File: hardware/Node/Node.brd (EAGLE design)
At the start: 49.5 x 49.5 mm, 71 parts, among them J1 AVR_SPI_PRG_6NS, J2 M04X2, Q1 PMR280UN, Q2 PMR280UN, Q3 PMR280UN, SW1 KSS, SW2 KSS, U1 ATMEGA32U4QFN, U2 BLUETOOTH-RN41", U3 LSM303DLM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

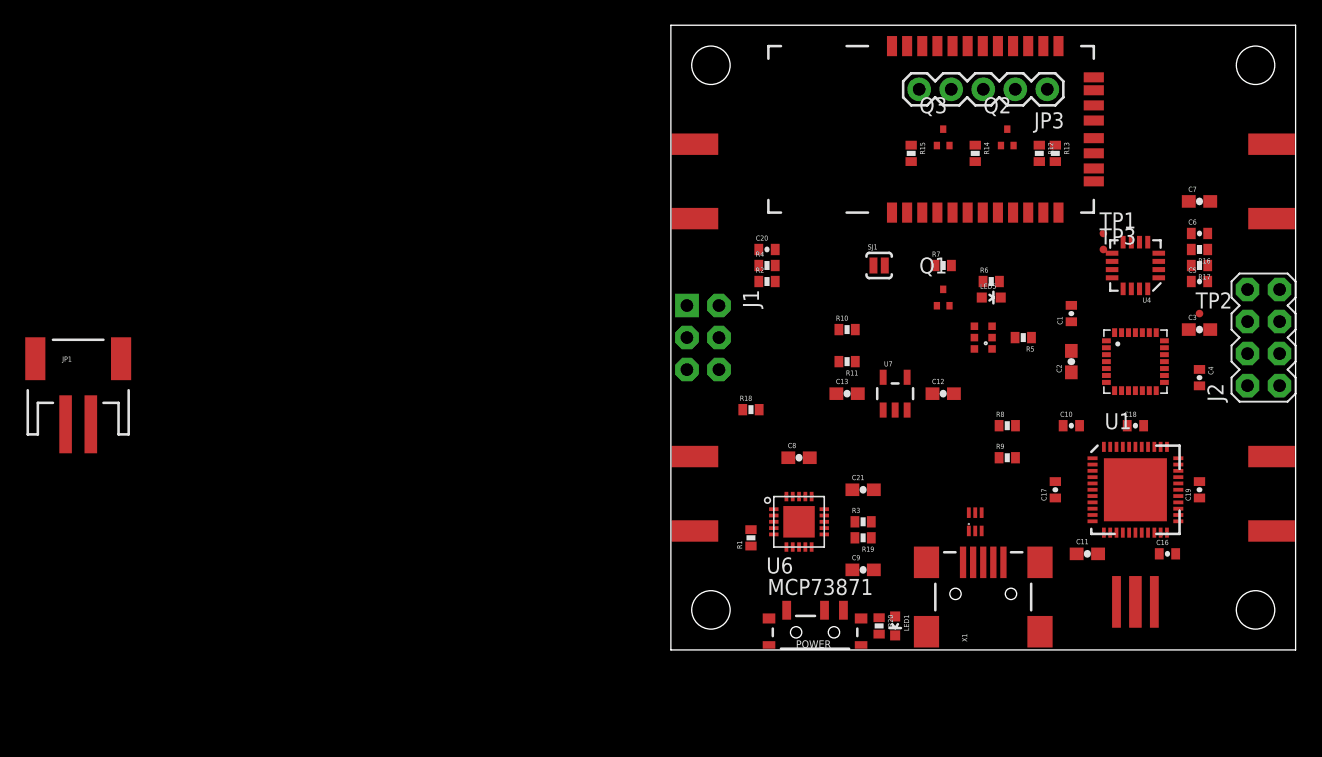
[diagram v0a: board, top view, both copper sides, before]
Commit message: put vbus on the header
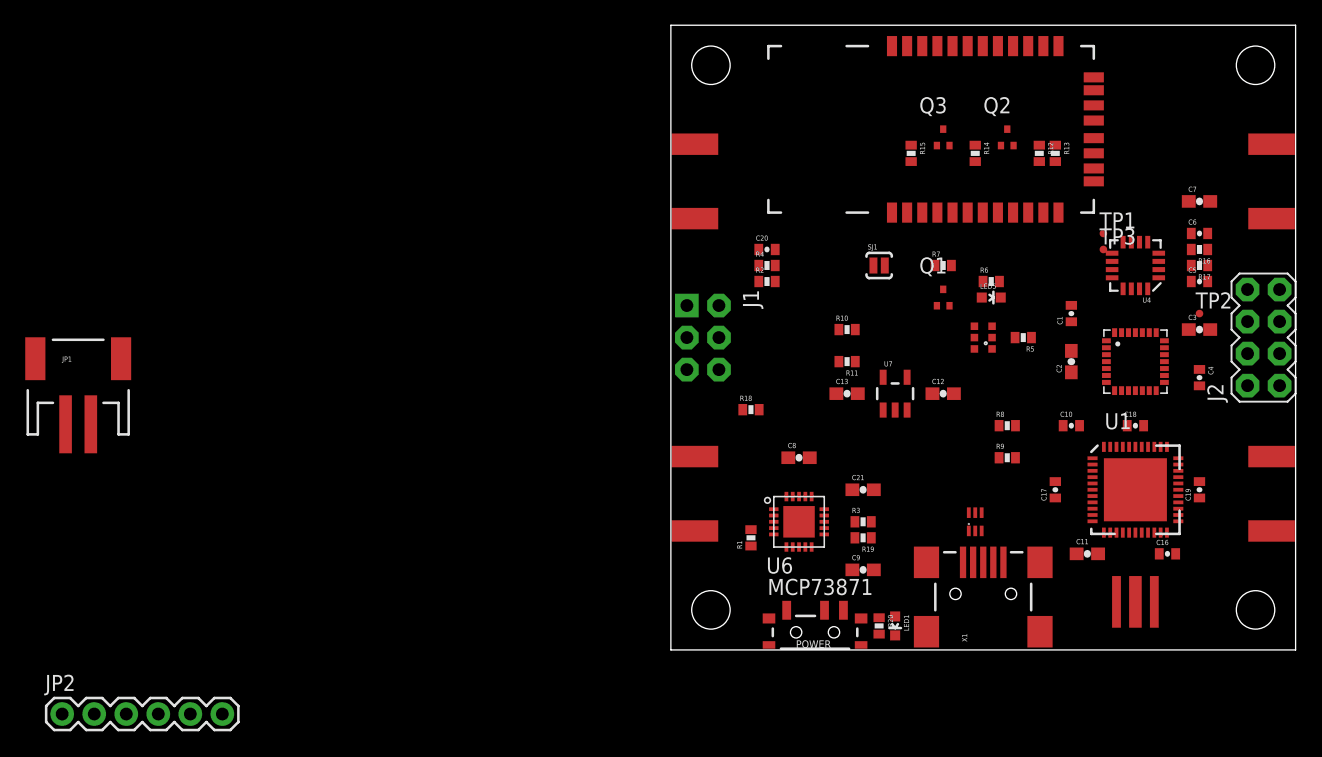
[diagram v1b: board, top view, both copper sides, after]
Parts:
- removed JP3: (no value), SparkFun:1X05
- added JP2: (no value), SparkFun:1X06
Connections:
- net +3V3: now also JP2.2; no longer JP3.1
- net GND: now also JP2.6; no longer JP3.5
- net RX_I: now also JP2.4; no longer JP3.3
- net TX_O: now also JP2.5; no longer JP3.4
- net VBUS: now also JP2.1
- net VIN: now also JP2.3; no longer JP3.2

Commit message: Start of laying out traces
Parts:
- moved JP2 81.1 mm to (17.8, 41.9)
- moved JP1 56.6 mm to (9.53, 24.8), turned to 90 degrees
- moved LED1 16.7 mm to (1.91, 6.99), turned to 270 degrees
- moved C5 15.2 mm to (41.9, 44.5), turned to 90 degrees
- moved R20 14.5 mm to (5.08, 10.8)
- moved R10 12.5 mm to (20.3, 14.6)
- moved R11 12.0 mm to (20.3, 12.7)
- moved C6 11.5 mm to (40.6, 44.5), turned to 90 degrees
- moved U4 10.8 mm to (41.9, 40.0), turned to 0 degrees
- moved R15 9.52 mm to (28.6, 39.4), turned to 180 degrees
- moved C7 9.44 mm to (38.7, 44.5), turned to 90 degrees
- moved TP1 9.25 mm to (43.2, 35.6)
- moved Q3 9.09 mm to (29.8, 44.5), turned to 90 degrees
- moved C13 8.98 mm to (20.3, 26.7)
- moved C8 7.75 mm to (14.6, 8.89)
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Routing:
- net VBUS: track 0.00 -> 13.0 mm
- net N$4: track 0.00 -> 7.32 mm
- net N$2: track 0.00 -> 6.11 mm
- net N$1: track 0.00 -> 5.90 mm
- net N$13: track 0.00 -> 4.47 mm
- net N$16: track 0.00 -> 2.69 mm
- net D-: track 0.00 -> 2.50 mm
- net D+: track 0.00 -> 2.49 mm
- net N$36: track 0.00 -> 2.49 mm
- net N$19: track 0.00 -> 2.45 mm
- added copper zone on layer 1, net N$11
- added copper zone on layer 1, net N$4
- added copper zone on layer 1, net VBUS

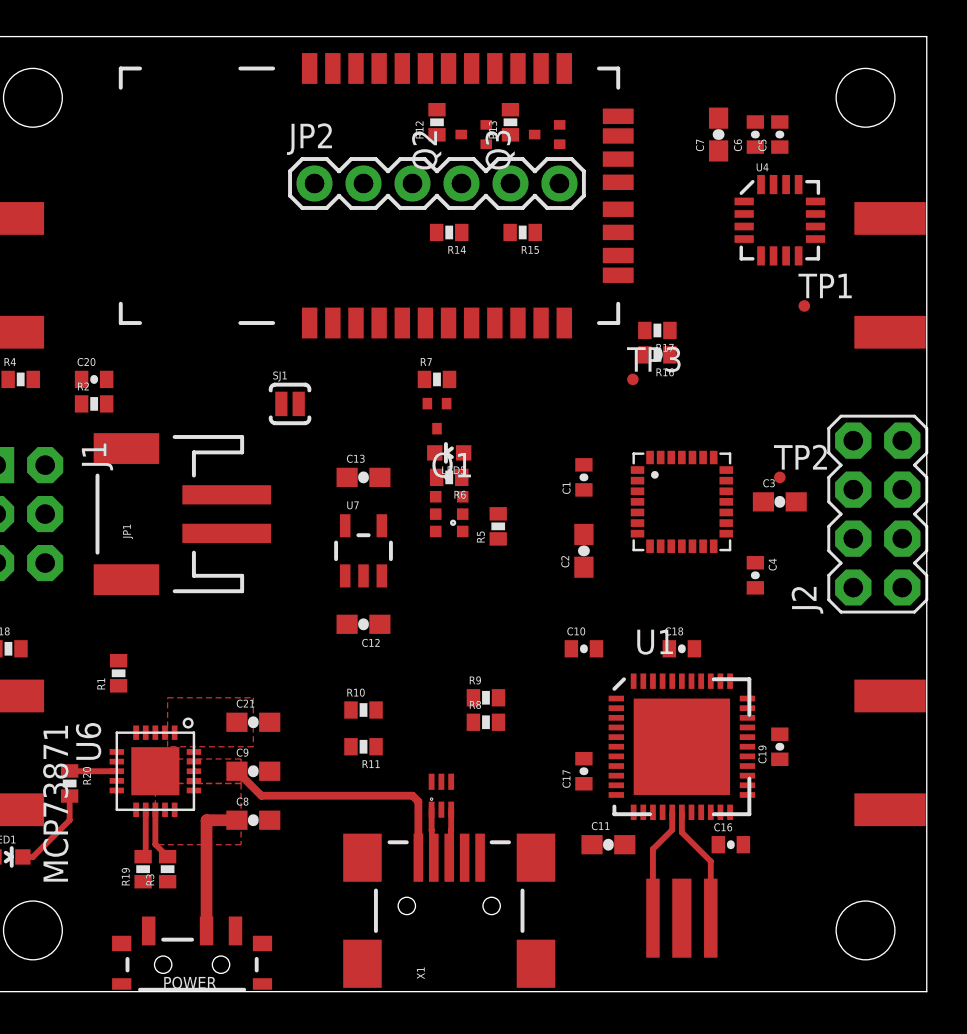
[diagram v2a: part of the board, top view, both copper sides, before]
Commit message: Routing more of the easy traces
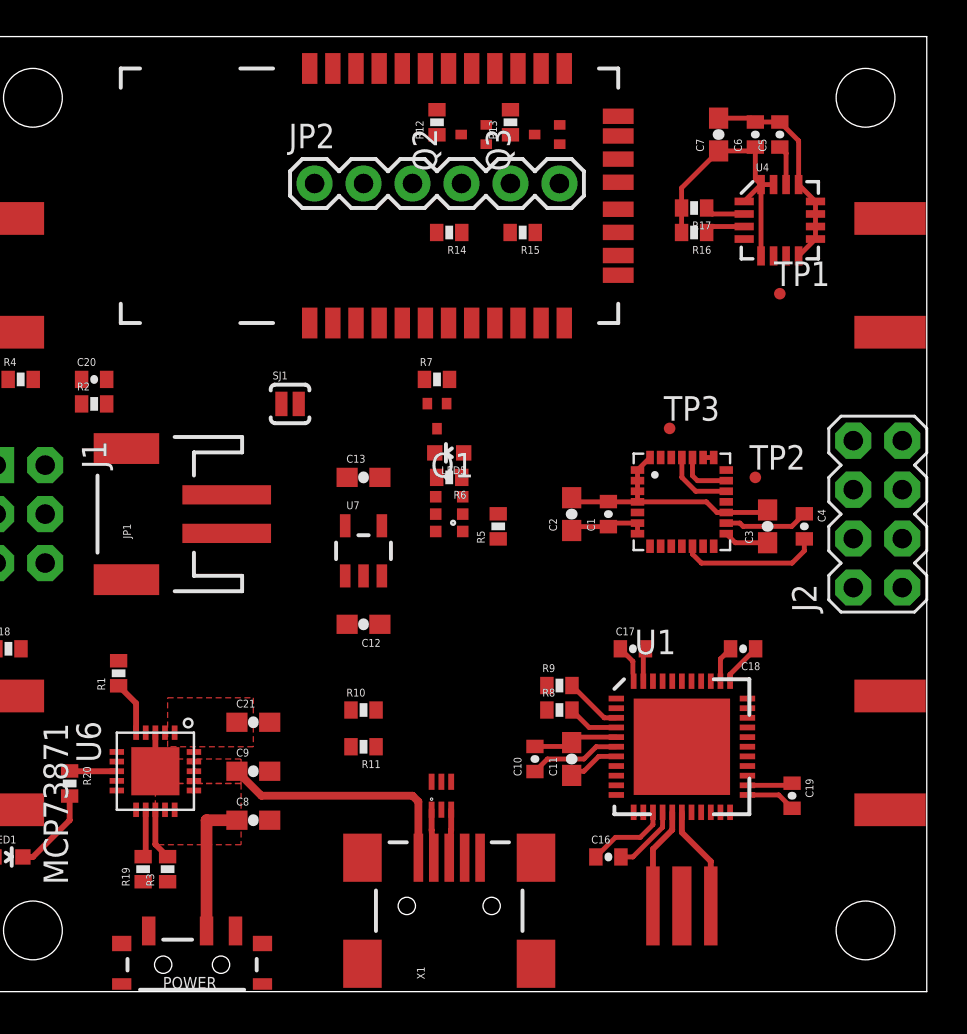
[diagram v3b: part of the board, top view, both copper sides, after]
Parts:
- moved C17 6.84 mm to (34.3, 17.8), turned to 0 degrees
- moved R17 6.63 mm to (37.5, 40.6)
- moved R16 6.63 mm to (37.5, 39.4)
- moved C16 6.38 mm to (33.0, 6.99)
- moved C10 6.25 mm to (29.2, 12.1), turned to 90 degrees
- moved C11 4.84 mm to (31.1, 12.1), turned to 90 degrees
- moved R8 3.86 mm to (30.5, 14.6)
- moved R9 3.86 mm to (30.5, 15.9)
- moved C4 3.59 mm to (43.2, 24.1)
- moved C18 3.18 mm to (40.0, 17.8), turned to 180 degrees
- moved TP3 3.18 mm to (36.2, 29.2)
- moved C19 2.62 mm to (42.5, 10.2), turned to 270 degrees
- moved C1 2.29 mm to (33.0, 24.8)
- moved C2 2.01 mm to (31.1, 24.8)
- moved TP1 1.42 mm to (41.9, 36.2)
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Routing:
- net GND: track 0.00 -> 40.6 mm
- net +3V3: track 0.00 -> 34.5 mm
- net N$6: track 0.00 -> 7.29 mm
- net SDA: track 0.00 -> 5.70 mm
- net SCL: track 0.00 -> 4.89 mm
- net N$5: track 0.00 -> 4.39 mm
- net N$24: track 0.00 -> 2.99 mm
- net N$8: track 0.00 -> 2.80 mm
- net VBUS: track 13.0 -> 15.7 mm
- net N$23: track 0.00 -> 2.69 mm
- net N$3: track 0.00 -> 2.34 mm
- net N$7: track 0.00 -> 2.08 mm
- net N$2: track 6.11 -> 5.48 mm
- net N$1: track 5.90 -> 5.27 mm

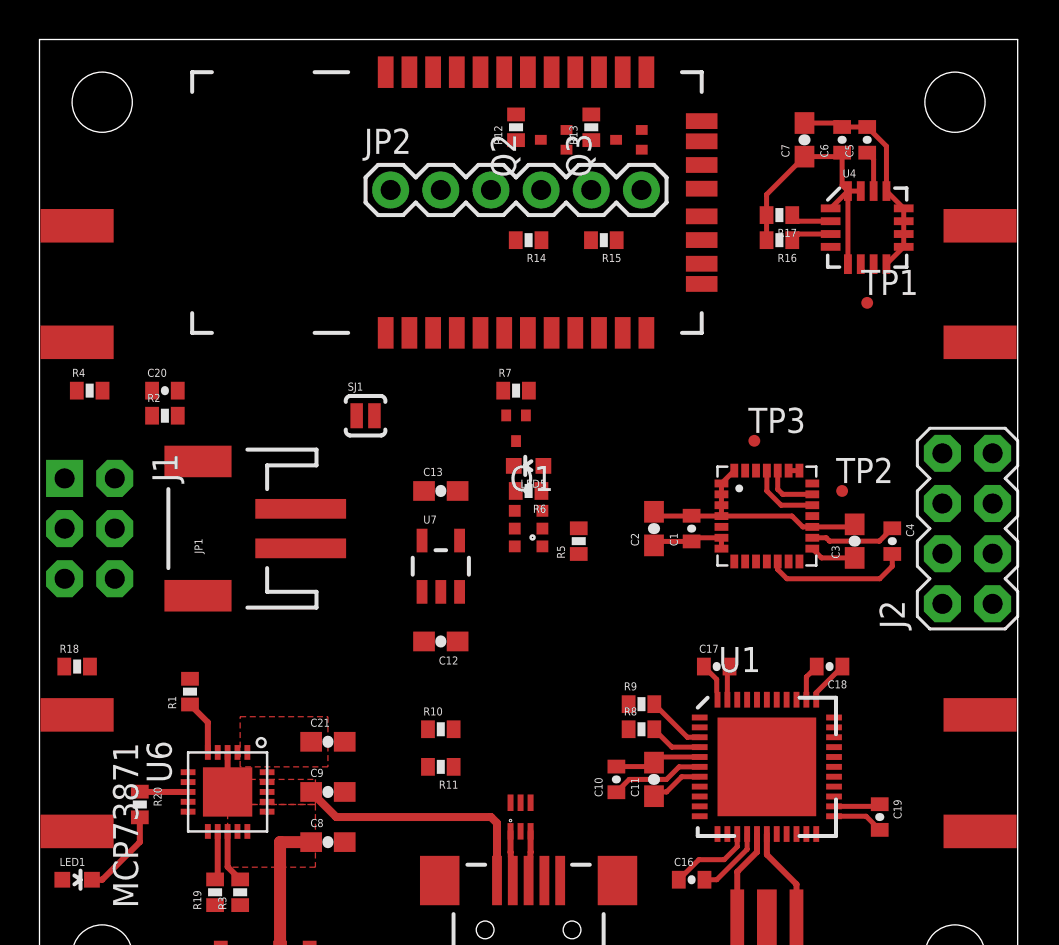
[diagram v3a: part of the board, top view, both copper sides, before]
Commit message: route more of the breakouts
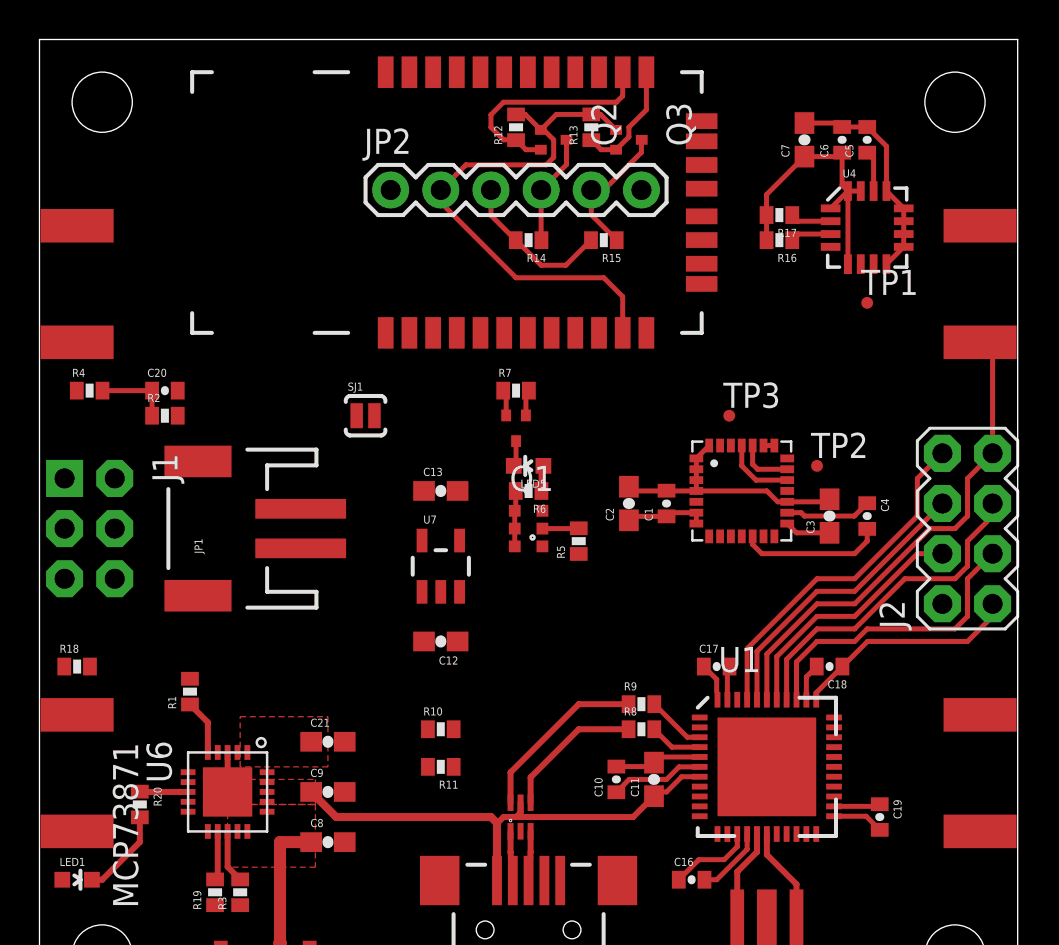
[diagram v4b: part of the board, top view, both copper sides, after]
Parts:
- moved RESET 52.0 mm to (1.91, 37.1), turned to 270 degrees
- moved SW1 52.0 mm to (47.6, 12.4), turned to 90 degrees
- moved C1 1.80 mm to (31.8, 26.0)
- moved C4 1.80 mm to (41.9, 25.4)
- moved TP2 1.80 mm to (39.4, 27.9)
- moved TP3 1.80 mm to (34.9, 30.5)
- moved C2 1.80 mm to (29.8, 26.0)
- moved U3 1.80 mm to (35.6, 26.7)
- moved C3 1.80 mm to (40.0, 25.4)
- turned Q2 to 270 degrees
- turned Q3 to 270 degrees
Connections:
- removed net N$31: J2.5, SW2.P$1, U1.37
- removed net N$33: J2.4, U1.39
- new net N$15: J2.4, U1.38
- new net N$30: J2.7, SW2.P$1, U1.39
- net N$32: now also J2.5, U1.37; no longer J2.7, U1.38
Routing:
- net +3V3: track 34.5 -> 74.5 mm
- net N$30: track 0.00 -> 24.8 mm
- net N$35: track 0.00 -> 17.7 mm
- net N$32: track 0.00 -> 16.9 mm
- net N$28: track 0.00 -> 15.2 mm
- net N$34: track 0.00 -> 14.9 mm
- net N$15: track 0.00 -> 12.7 mm
- net RX: track 0.00 -> 11.9 mm
- net VBUS: track 15.7 -> 25.0 mm
- net N$26: track 0.00 -> 8.95 mm
- net VIN: track 0.00 -> 7.92 mm
- net N$25: track 0.00 -> 7.26 mm
- net TX_O: track 0.00 -> 7.04 mm
- net TX: track 0.00 -> 6.02 mm
- net RX_I: track 0.00 -> 5.62 mm
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
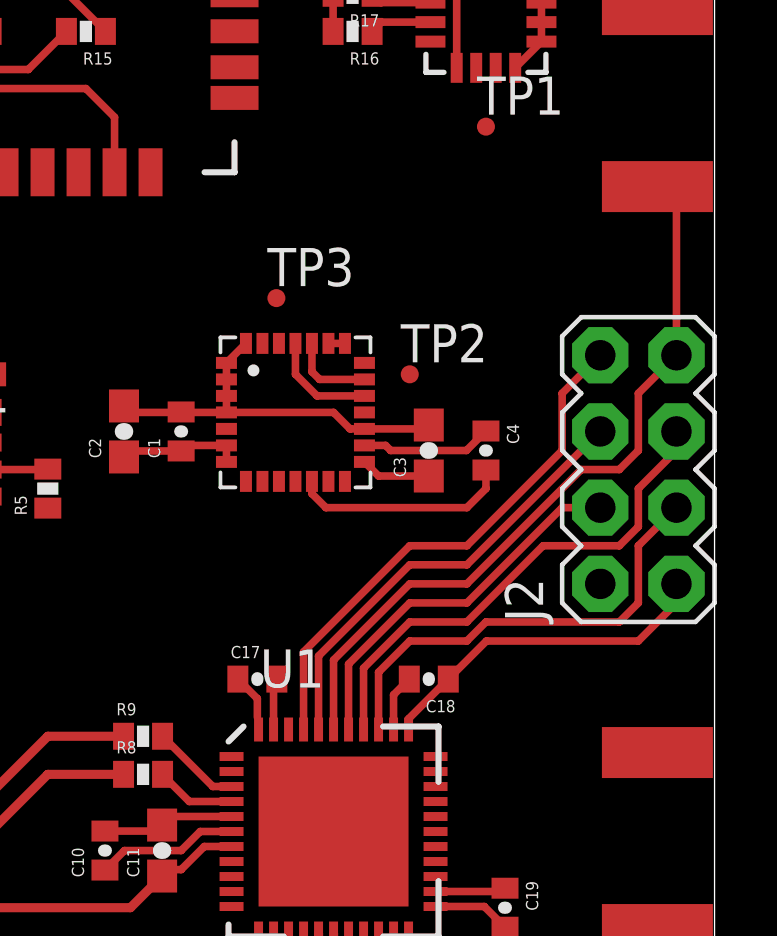
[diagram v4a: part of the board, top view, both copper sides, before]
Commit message: reorder some pins
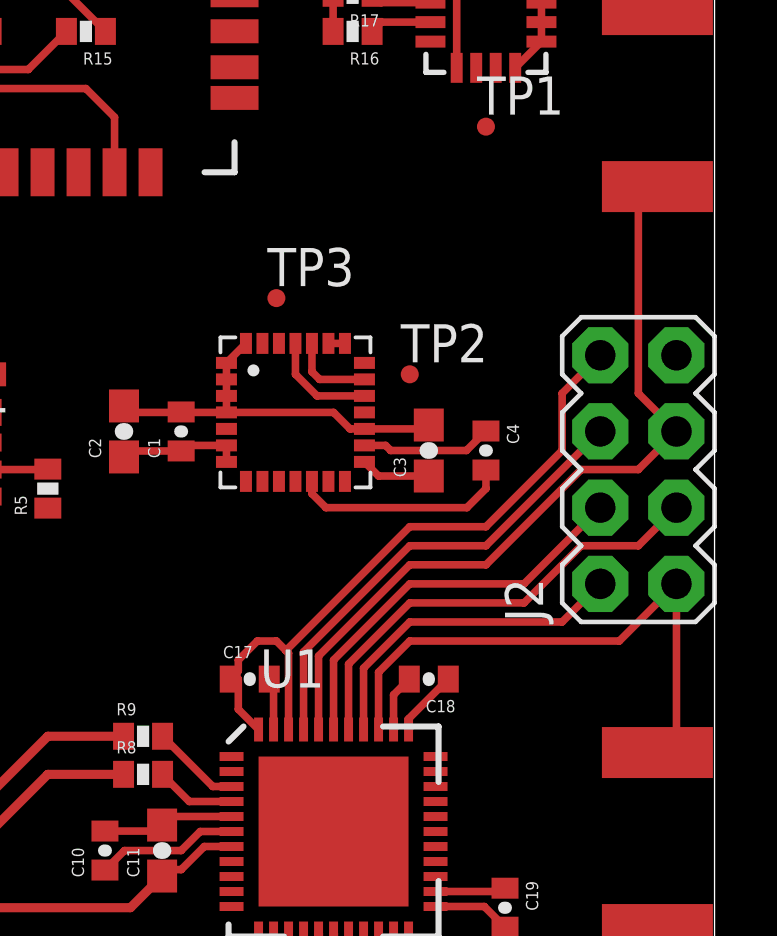
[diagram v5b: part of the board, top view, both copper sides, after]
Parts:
- moved C17 0.25 mm to (34.0, 17.8)
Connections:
- removed net N$15: J2.4, U1.38
- new net N$33: J2.4, U1.39
- net +3V3: now also J2.8; no longer J2.1
- net GND: now also J2.7, SW1.P$1; no longer J2.2, SW1.P$2
- net N$28: now also J2.1, SW1.P$2; no longer J2.3, SW1.P$1
- net N$30: now also J2.2, U1.37; no longer J2.7, SW2.P$1, U1.39
- net N$32: now also J2.3, U1.38; no longer J2.5, U1.37
- net N$34: now also J2.5, SW2.P$1; no longer J2.6
- net N$35: now also J2.6; no longer J2.8
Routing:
- net N$30: track 24.8 -> 11.1 mm
- net N$33: track 0.00 -> 13.3 mm
- net N$15: track 12.7 -> 0.00 mm
- net +3V3: track 74.5 -> 86.9 mm
- net N$34: track 14.9 -> 26.4 mm
- net N$28: track 15.2 -> 18.9 mm
- net N$35: track 17.7 -> 15.5 mm
- net N$32: track 16.9 -> 15.3 mm
